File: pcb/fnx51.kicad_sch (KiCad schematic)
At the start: 22 parts

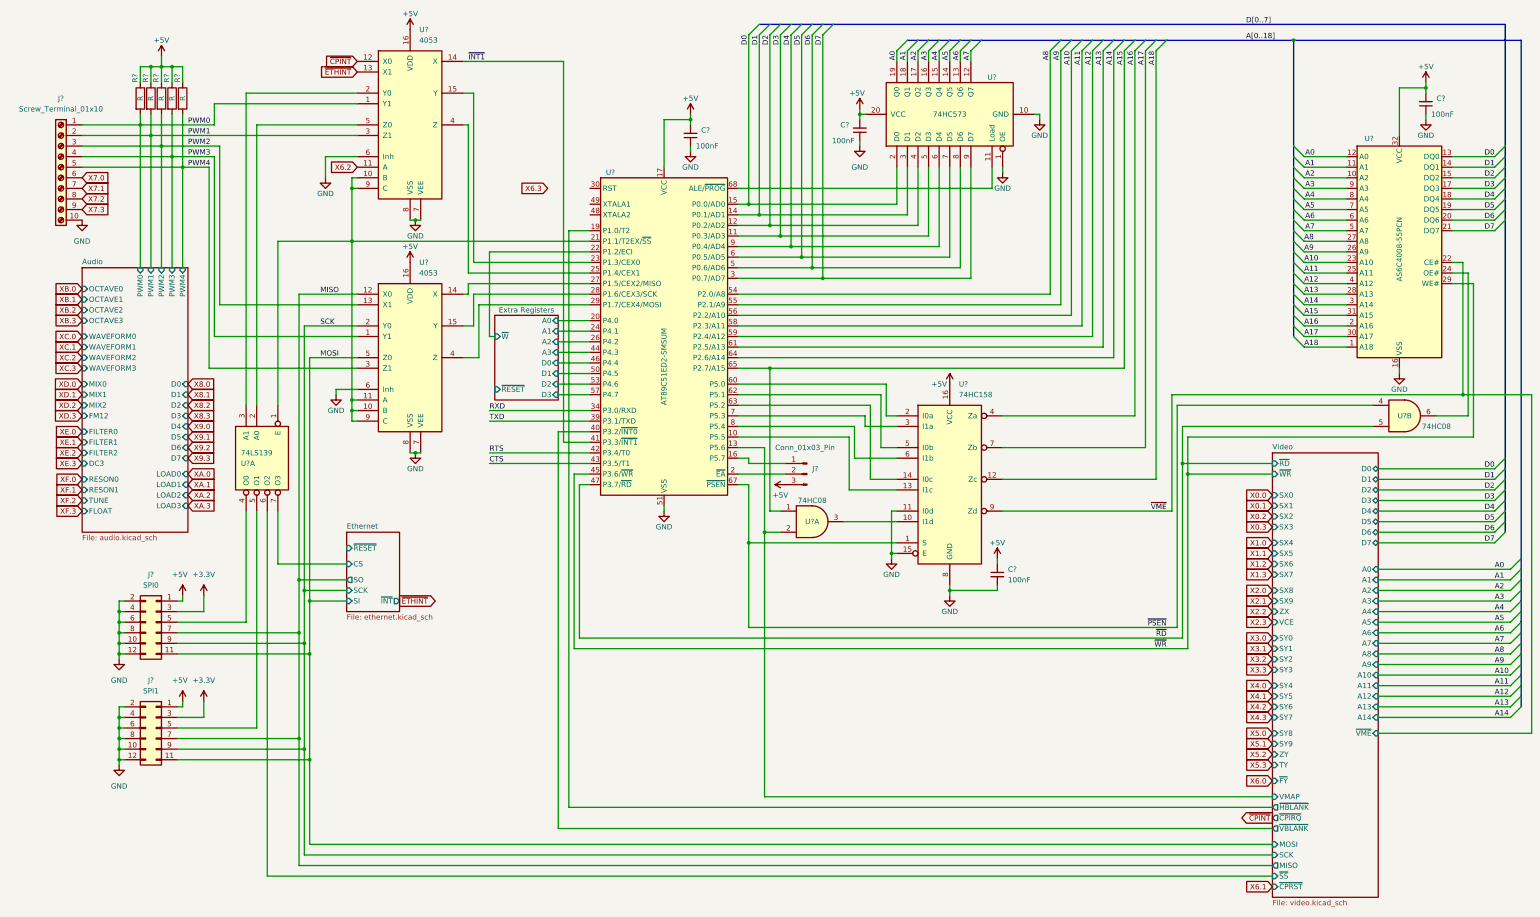
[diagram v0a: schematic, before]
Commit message: PCB: add reset circuit, xtal
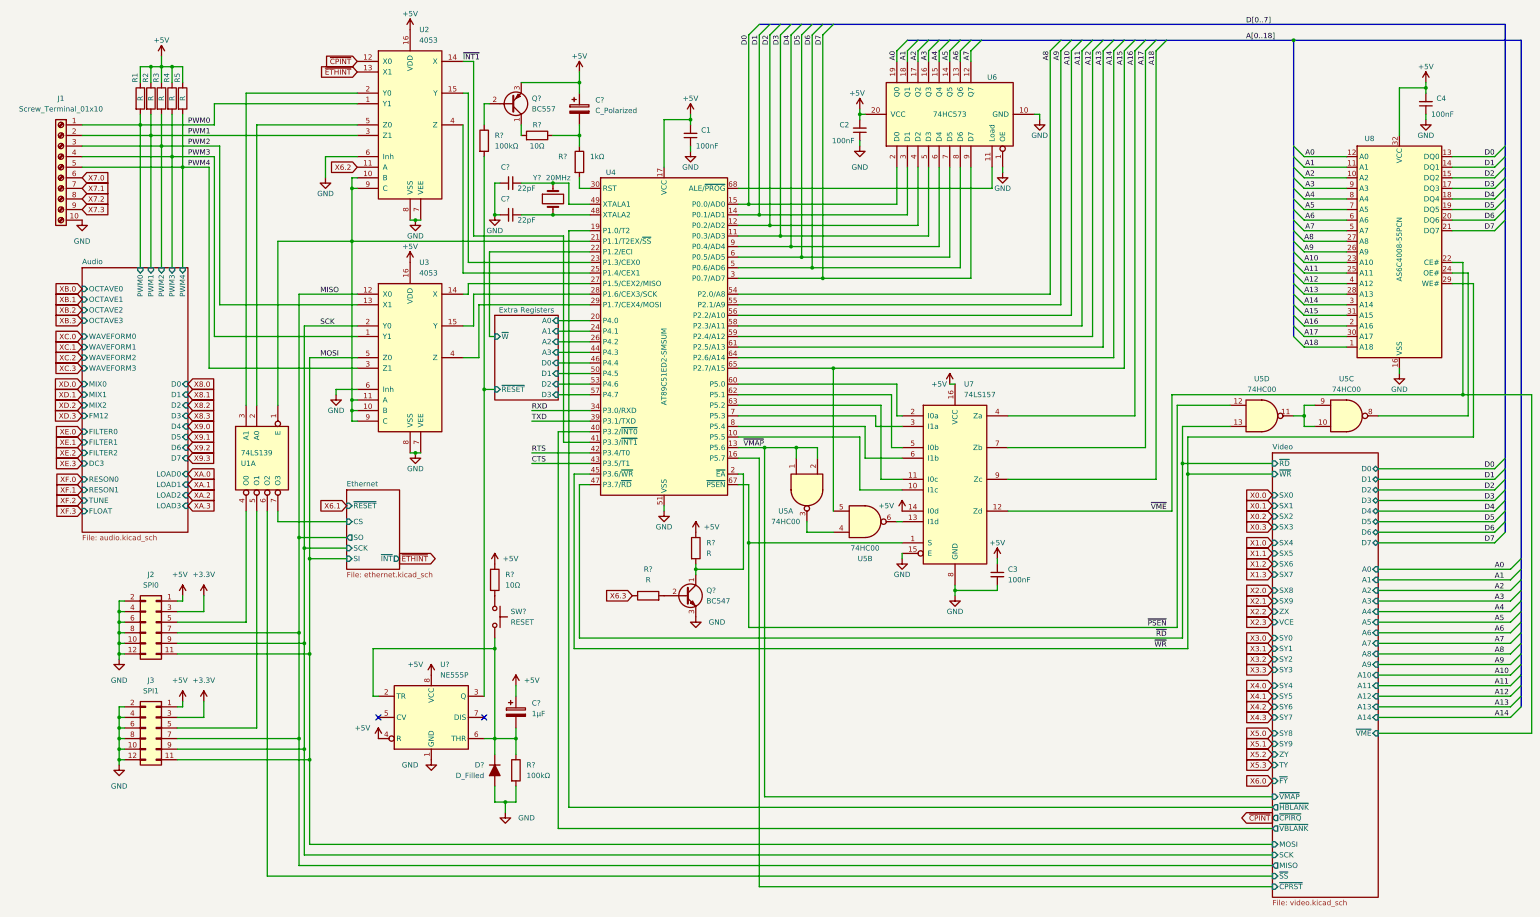
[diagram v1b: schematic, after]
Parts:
- removed J?: Conn_01x03_Pin, symbol Connector:Conn_01x03_Pin
- removed U?: 74HC158, symbol 74xx:74LS158
- removed U? (x2): 74HC08, symbol 74xx:74LS08
- added C?: 1µF, symbol Device:C_Polarized
- added C? (x2): 22pF, symbol Device:C_Small
- added C?: C_Polarized, symbol Device:C_Polarized
- added D?: D_Filled, symbol Device:D_Filled
- added Q?: BC557, Package_TO_SOT_THT:TO-92_Inline, symbol Transistor_BJT:BC557
- added Q?: BC547, Package_TO_SOT_THT:TO-92_Inline, symbol Transistor_BJT:BC547
- added R? (x2): 10Ω, symbol Device:R
- added R? (x2): 100kΩ, symbol Device:R
- added R?: 1kΩ, symbol Device:R
- added R? (x2): R, symbol Device:R
- added SW?: RESET, symbol Switch:SW_Push
- added U5: 74HC00, symbol 74xx:74HC00
- added U7: 74LS157, symbol 74xx:74LS157
- added U?: NE555P, Package_DIP:DIP-8_W7.62mm, symbol Timer:NE555P
- added Y?: 20MHz, symbol Device:Crystal
- gave numbers to parts that had none: 18
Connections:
- net +5V: now also C?.1, C?.1, Q?.3 (E), R?.1, R?.1, U7.14 (I0d), U7.16 (VCC), U?.4 (R), U?.8 (VCC)
- net A15: now also U5.5
- net A16: now also U7.4 (Za)
- net A17: now also U7.7 (Zb)
- net A18: now also U7.9 (Zc)
- net Extra Registers/~{RESET}: now also R?.2, U?.3 (Q)
- net GND: now also C?.1, C?.2, D?.2 (A), Q?.3 (E), R?.2, U7.15 (E), U7.8 (GND), U?.1 (GND)
- net X6.3: now also R?.1
- net ~{PSEN}: now also U5.12, U7.1 (S)
- net ~{RD}: now also U5.13
- net ~{VME}: now also U7.12 (Zd)
- net at U4.10 (P5.5): now also U7.10 (I1c)
- net Video/~{CPRST}: now reaches U4.16 (P5.7)
- net at U4.2 (~{EA}): now also Q?.1 (C), R?.2
- net at U4.30 (RST): now also R?.2
- net at U4.48 (XTALA2): now also C?.1, Y?.2
- net at U4.49 (XTALA1): now also C?.2, Y?.1
- net at U4.60 (P5.0): now also U7.2 (I0a)
- net at U4.62 (P5.1): now also U7.5 (I0b)
- net at U4.63 (P5.2): now also U7.11 (I0c)
- net at U4.7 (P5.3): now also U7.3 (I1a)
- net at U4.8 (P5.4): now also U7.6 (I1b)
- net at U8.24 (OE#): now also U5.8
- net Video/VMAP renamed ~{VMAP}
- net ~{VMAP}: now also U5.1, U5.2
- new net: Q?.1 (C), R?.2
- new net: Q?.2 (B), R?.1
- new net: U5.10, U5.11, U5.9
- new net: C?.2, D?.1 (K), R?.1, SW?.2, U?.2 (TR), U?.6 (THR)
- new net: U5.3, U5.4
- new net: U5.6, U7.13 (I1d)
- new net: R?.2, SW?.1
- new net: C?.2, R?.1, R?.1
- new net: Q?.2 (B), R?.2
- no-connect marks 0 -> 2
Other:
- sheet Video ports: added ~{VMAP}; removed VMAP

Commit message: WIP schematic
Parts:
- added J2: ATX-24, symbol Connector:ATX-24
- added Q1: BC557, Package_TO_SOT_THT:TO-92_Inline, symbol Transistor_BJT:BC557
- added SW1: POWER, symbol Switch:SW_SPST
- U8: renamed from U7; value 74LS157 -> 74HC157
- gave numbers to parts that had none: 17
- renumbered C1 to C5, C2 to C6, C3 to C7, C4 to C8, J2 to J3, J3 to J4, U4 to U5, U5 to U6, U6 to U7, U8 to U9
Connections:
- net +3.3V: now also J2.1 (+3.3V), J2.12 (+3.3V), J2.13 (+3.3V), J2.2 (+3.3V)
- net +5V: now also J2.21 (+5V), J2.22 (+5V), J2.23 (+5V), J2.4 (+5V), J2.6 (+5V)
- net GND: now also J2.15 (GND), J2.17 (GND), J2.18 (GND), J2.19 (GND), J2.24 (GND), J2.3 (GND), J2.5 (GND), J2.7 (GND), SW1.1 (A)
- net at C3.2, D1.1 (K), R8.1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: now also Q1.1 (C)
- net at R7.2, SW2.1: now also Q1.3 (E)
- new net: J2.16 (PS_ON#), SW1.2 (B)
- new net: J2.8 (PWR_OK), Q1.2 (B)
- new net +12V: J2.10 (+12V), J2.11 (+12V)
- new net -12V: J2.14 (-12V)
- no-connect marks 2 -> 3
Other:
- moved on the sheet: R7, SW2

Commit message: WIP schematic
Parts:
- added U1: 74HCT125, symbol 74xx:74LS125
- U2: renamed from U1; value 74LS139 -> 74HC139
- renumbered J3 to J2, J4 to J3, J2 to J4, U9 to U10, U2 to U3, U3 to U4, U4 to U5, U5 to U6, U6 to U7, U7 to U8, U8 to U9
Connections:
- net MISO: now also U1.11, U1.8; no longer J2.7 (Pin_7), J3.7 (Pin_7)
- net at J2.5 (Pin_5), U2.4 (O0): now also U1.10
- net at J3.5 (Pin_5), U2.5 (O1): now also U1.13
- new net: J3.7 (Pin_7), U1.12
- new net: J2.7 (Pin_7), U1.9
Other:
- moved on the sheet: J2, J3

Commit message: WIP schematic
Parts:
- added C1, C5, C7: 100nF, symbol Device:C_Small
- added unit 5 of U1
- added unit 3 of U2
- added unit 5 of U6
- renumbered C7 to C10, C8 to C11, C1 to C2, C2 to C3, C3 to C4, C4 to C6, C5 to C8, C6 to C9, U7 to U6, U6 to U7
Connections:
- net +5V: now also C1.2, C5.2, C7.2, U1.14 (VCC), U2.16 (VCC), U6.7 (GND)
- net GND: now also C1.1, C5.1, C7.1, U1.7 (GND), U2.8 (GND), U6.14 (VCC)
- net CTS renamed Serial Port/RTS
- net RTS renamed Serial Port/CTS
- net RXD renamed Serial Port/RXD
- net TXD renamed Serial Port/TXD
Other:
- added sheet Serial Port (serial.kicad_sch)

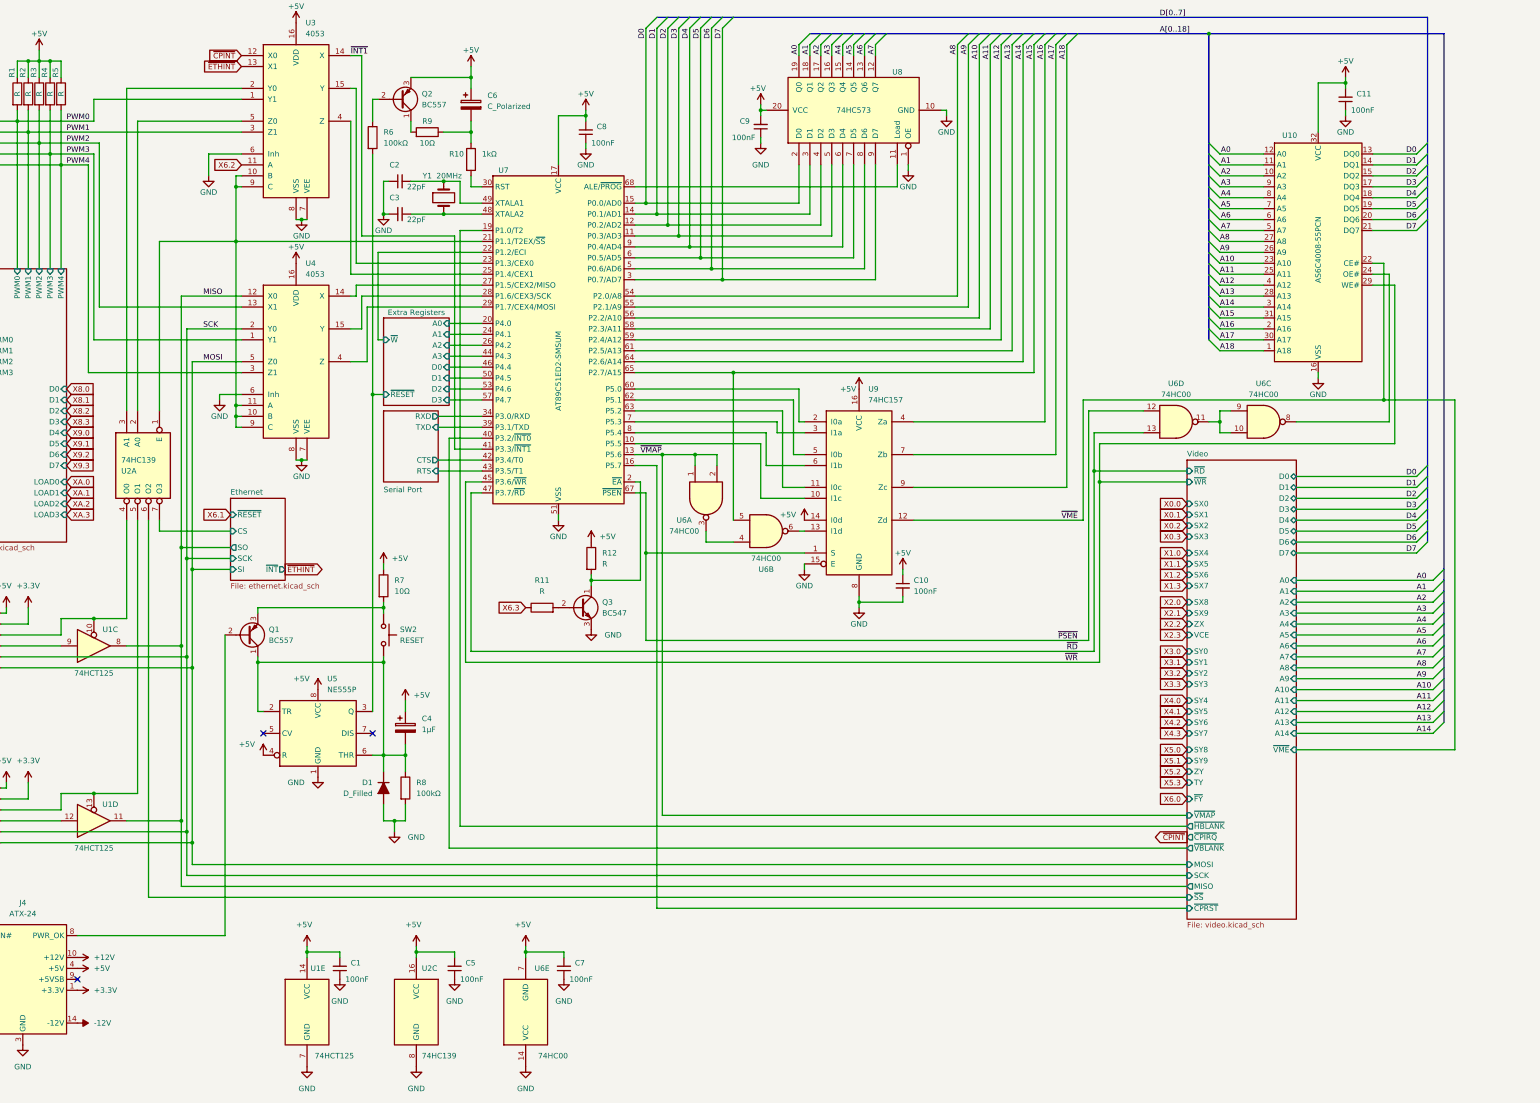
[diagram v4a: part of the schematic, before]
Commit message: WIP PCB (add bypass caps, minor fixes)
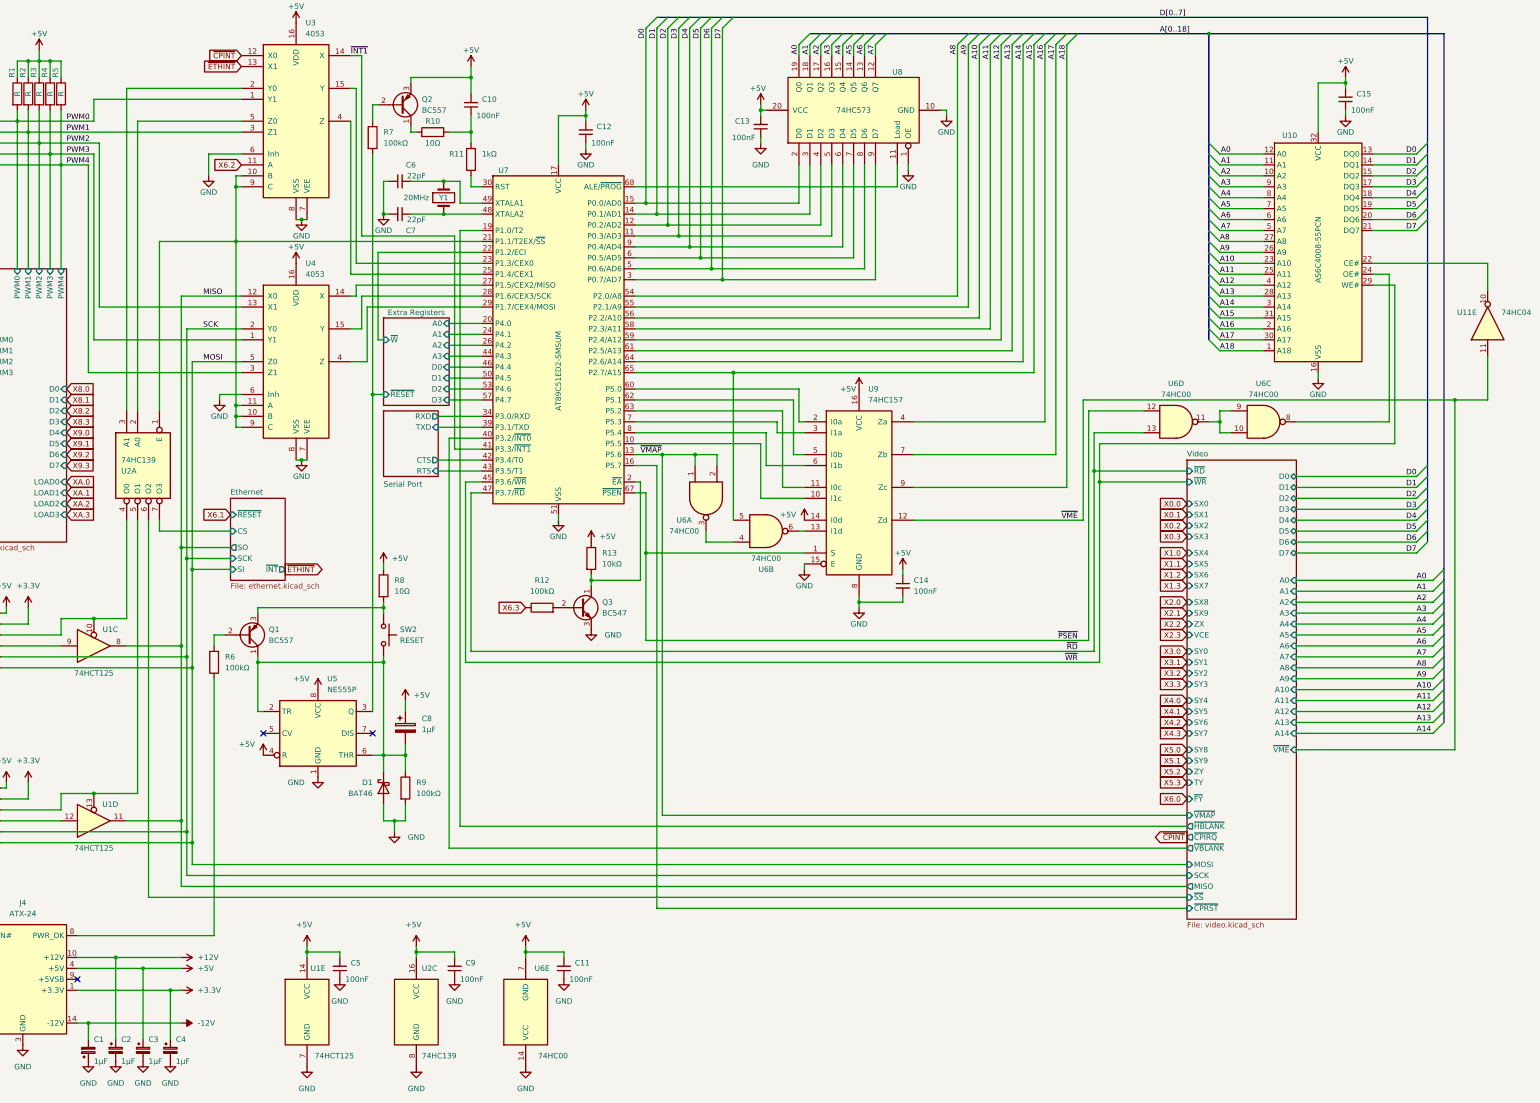
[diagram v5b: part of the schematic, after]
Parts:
- removed C6: C_Polarized, symbol Device:C_Polarized
- added C1, C2, C3, C4: 1µF, symbol Device:C_Polarized_Small
- added C10: 100nF, symbol Device:C_Small
- added R6: 100kΩ, symbol Device:R
- added U11: 74HC04, symbol 74xx:74HC04
- D1: value D_Filled -> BAT46; footprint (none) -> Diode_THT:D_DO-35_SOD27_P7.62mm_Horizontal; symbol Device:D_Filled -> Diode:BAT46
- R12: renamed from R11; value R -> 100kΩ
- R13: renamed from R12; value R -> 10kΩ
- renumbered C7 to C11, C8 to C12, C9 to C13, C10 to C14, C11 to C15, C1 to C5, C2 to C6, C3 to C7, C4 to C8, C5 to C9, R9 to R10, R10 to R11, R6 to R7, R7 to R8, R8 to R9
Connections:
- net +12V: now also C2.1
- net +3.3V: now also C4.1
- net +5V: now also C10.2, C3.1
- net -12V: now also C1.2
- net GND: now also C1.1, C2.2, C3.2, C4.2
- net ~{VME}: now also U11.11; no longer U10.22 (CE#)
- net at R10.1, R11.1: now also C10.1
- net at Q1.2 (B): now also R6.2; no longer J4.8 (PWR_OK)
- new net: U10.22 (CE#), U11.10
- new net: J4.8 (PWR_OK), R6.1
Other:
- moved on the sheet: Q2, R10
